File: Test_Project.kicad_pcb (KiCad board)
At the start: 2 copper layers, 4 parts, among them U1 STM32L081KZTx, U2 MIC2132YML

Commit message: Finished up schematic
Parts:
- added C10: 100nF, Test_Project_Lib:C_0603_1608Metric_Pad1.08x0.95mm_HandSolder, F.Cu at (116.6, 49.5)
- added C11: 1uF, Test_Project_Lib:C_0603_1608Metric_Pad1.08x0.95mm_HandSolder, F.Cu at (121.0, 39.5)
- added C12: 100nF, Test_Project_Lib:C_0603_1608Metric_Pad1.08x0.95mm_HandSolder, F.Cu at (121.0, 42.0)
- added C13: 1uF, Test_Project_Lib:C_0603_1608Metric_Pad1.08x0.95mm_HandSolder, F.Cu at (121.0, 44.5)
- added C14: 100nF, Test_Project_Lib:C_0603_1608Metric_Pad1.08x0.95mm_HandSolder, F.Cu at (121.0, 47.0)
- added C15: 22uF, Test_Project_Lib:C_0805_2012Metric_Pad1.18x1.45mm_HandSolder, F.Cu at (112.1, 27.9)
- added C16: 22uF, Test_Project_Lib:C_0805_2012Metric_Pad1.18x1.45mm_HandSolder, F.Cu at (112.1, 30.9)
- added C17: 100nF, Test_Project_Lib:C_0603_1608Metric_Pad1.08x0.95mm_HandSolder, F.Cu at (121.0, 49.5)
- added C18: ?uF, Test_Project_Lib:C_0603_1608Metric_Pad1.08x0.95mm_HandSolder, F.Cu at (125.3, 39.5)
- added C19: 4.7uF, Test_Project_Lib:C_0603_1608Metric_Pad1.08x0.95mm_HandSolder, F.Cu at (125.3, 42.0)
- added C2: 100nF, Test_Project_Lib:C_0603_1608Metric_Pad1.08x0.95mm_HandSolder, F.Cu at (169.1, 30.9)
- added C20: 4.7uF, Test_Project_Lib:C_0603_1608Metric_Pad1.08x0.95mm_HandSolder, F.Cu at (125.3, 44.5)
- added C21: 22uF, Test_Project_Lib:C_0805_2012Metric_Pad1.18x1.45mm_HandSolder, F.Cu at (112.1, 33.9)
- added C22: 22uF, Test_Project_Lib:C_0805_2012Metric_Pad1.18x1.45mm_HandSolder, F.Cu at (112.1, 36.9)
- added C23: 22uF, Test_Project_Lib:C_0805_2012Metric_Pad1.18x1.45mm_HandSolder, F.Cu at (112.1, 40.0)
- added C24: 22uF, Test_Project_Lib:C_0805_2012Metric_Pad1.18x1.45mm_HandSolder, F.Cu at (112.1, 43.0)
- added C25: 22uF, Test_Project_Lib:C_0805_2012Metric_Pad1.18x1.45mm_HandSolder, F.Cu at (112.1, 46.0)
- added C26: 22uF, Test_Project_Lib:C_0805_2012Metric_Pad1.18x1.45mm_HandSolder, F.Cu at (112.1, 49.0)
- added C27: 100uF, Test_Project_Lib:CP_Radial_D6.3mm_P2.50mm, F.Cu at (130.3, 42.1)
- added C28: 100nF, Test_Project_Lib:C_0603_1608Metric_Pad1.08x0.95mm_HandSolder, F.Cu at (142.7, 64.8)
- added C29: 1uF, Test_Project_Lib:C_0603_1608Metric_Pad1.08x0.95mm_HandSolder, F.Cu at (142.7, 67.3)
- added C3: 100nF, Test_Project_Lib:C_0603_1608Metric_Pad1.08x0.95mm_HandSolder, F.Cu at (169.1, 33.4)
- added C30: 1uF, Test_Project_Lib:C_0603_1608Metric_Pad1.08x0.95mm_HandSolder, F.Cu at (142.7, 69.8)
- added C31: 1uF, Test_Project_Lib:C_0603_1608Metric_Pad1.08x0.95mm_HandSolder, F.Cu at (169.1, 40.9)
- added C32: 1uF, Test_Project_Lib:C_0603_1608Metric_Pad1.08x0.95mm_HandSolder, F.Cu at (169.1, 43.4)
- added C4: 100nF, Test_Project_Lib:C_0603_1608Metric_Pad1.08x0.95mm_HandSolder, F.Cu at (169.1, 35.9)
- added C5: 1uF, Test_Project_Lib:C_0603_1608Metric_Pad1.08x0.95mm_HandSolder, F.Cu at (169.1, 38.4)
- added C6: 100pF, Test_Project_Lib:C_0603_1608Metric_Pad1.08x0.95mm_HandSolder, F.Cu at (116.6, 39.5)
- added C7: 100nF, Test_Project_Lib:C_0603_1608Metric_Pad1.08x0.95mm_HandSolder, F.Cu at (116.6, 42.0)
- added C8: 1uF, Test_Project_Lib:C_0603_1608Metric_Pad1.08x0.95mm_HandSolder, F.Cu at (116.6, 44.5)
- added C9: 100nF, Test_Project_Lib:C_0603_1608Metric_Pad1.08x0.95mm_HandSolder, F.Cu at (116.6, 47.0)
- added J2: Conn_01x02, Test_Project_Lib:PinHeader_1x02_P2.54mm_Vertical, F.Cu at (183.3, 69.4)
- added J3: Conn_01x03, Test_Project_Lib:PinHeader_1x03_P2.54mm_Vertical, F.Cu at (112.0, 64.9)
- added J4: Conn_01x03, Test_Project_Lib:PinHeader_1x03_P2.54mm_Vertical, F.Cu at (187.5, 29.4)
- added J5: Conn_01x04, Test_Project_Lib:PinHeader_1x04_P2.54mm_Vertical, F.Cu at (178.3, 29.4)
- added J6: Conn_01x04, Test_Project_Lib:PinHeader_1x04_P2.54mm_Vertical, F.Cu at (182.9, 29.4)
- added R1: 100k, Test_Project_Lib:R_0805_2012Metric_Pad1.20x1.40mm_HandSolder, F.Cu at (173.7, 28.6)
- added R10: 100k, Test_Project_Lib:R_0805_2012Metric_Pad1.20x1.40mm_HandSolder, F.Cu at (121.6, 36.7)
- added R11: 100k, Test_Project_Lib:R_0805_2012Metric_Pad1.20x1.40mm_HandSolder, F.Cu at (126.3, 27.9)
- added R12: 100k, Test_Project_Lib:R_0805_2012Metric_Pad1.20x1.40mm_HandSolder, F.Cu at (126.3, 30.8)
- added R13: 2.2Ω, Test_Project_Lib:R_0805_2012Metric_Pad1.20x1.40mm_HandSolder, F.Cu at (126.3, 33.8)
- added R14: 3.3k, Test_Project_Lib:R_0805_2012Metric_Pad1.20x1.40mm_HandSolder, F.Cu at (126.3, 36.7)
- added R15: 25.5 kΩ, Test_Project_Lib:R_0805_2012Metric_Pad1.20x1.40mm_HandSolder, F.Cu at (173.7, 34.5)
- added R16: 10k, Test_Project_Lib:R_0805_2012Metric_Pad1.20x1.40mm_HandSolder, F.Cu at (173.7, 37.5)
- added R17: 10k, Test_Project_Lib:R_0805_2012Metric_Pad1.20x1.40mm_HandSolder, F.Cu at (173.7, 40.4)
- added R18: 25.5 kΩ, Test_Project_Lib:R_0805_2012Metric_Pad1.20x1.40mm_HandSolder, F.Cu at (116.7, 64.1)
- added R19: 25.5 kΩ, Test_Project_Lib:R_0805_2012Metric_Pad1.20x1.40mm_HandSolder, F.Cu at (116.7, 67.0)
- added R2: 10k, Test_Project_Lib:R_0805_2012Metric_Pad1.20x1.40mm_HandSolder, F.Cu at (116.8, 27.9)
- added R3: 10k, Test_Project_Lib:R_0805_2012Metric_Pad1.20x1.40mm_HandSolder, F.Cu at (116.8, 30.8)
- added R4: 25.5 kΩ, Test_Project_Lib:R_0805_2012Metric_Pad1.20x1.40mm_HandSolder, F.Cu at (116.8, 33.8)
- added R5: 25.5 kΩ, Test_Project_Lib:R_0805_2012Metric_Pad1.20x1.40mm_HandSolder, F.Cu at (116.8, 36.7)
- added R6: 100k, Test_Project_Lib:R_0805_2012Metric_Pad1.20x1.40mm_HandSolder, F.Cu at (121.6, 27.9)
- added R7: 3.3k, Test_Project_Lib:R_0805_2012Metric_Pad1.20x1.40mm_HandSolder, F.Cu at (121.6, 30.8)
- added R8: 100k, Test_Project_Lib:R_0805_2012Metric_Pad1.20x1.40mm_HandSolder, F.Cu at (173.7, 31.6)
- added R9: 10kΩ, Test_Project_Lib:R_0805_2012Metric_Pad1.20x1.40mm_HandSolder, F.Cu at (121.6, 33.8)
- added U3: ~, Test_Project_Lib:SOT-23W_Handsoldering, F.Cu at (148.3, 66.0)
- moved U2 78.2 mm to (132.4, 30.1)
- moved C1 62.8 mm to (169.1, 28.4)
- moved U1 34.2 mm to (181.7, 45.0)
- moved J1 14.1 mm to (175.3, 61.1)
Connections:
- net Net-(U1-NRST) renamed /nRST
- C1 pad 2: GNDREF -> <NO NET>
- J1 pad 1: unconnected-(J1-Pad1) -> /12V
- J1 pad 3: unconnected-(J1-Pad3) -> <NO NET>
- U1 pad 1: unconnected-(U1-VDD-Pad1) -> /VDD_3V3
- U1 pad 11: unconnected-(U1-PA5-Pad11) -> /SPI_SCK
- U1 pad 12: unconnected-(U1-PA6-Pad12) -> /SPI_MISO
- U1 pad 13: unconnected-(U1-PA7-Pad13) -> /SPI_MOSI
- U1 pad 16: Net-(U1-VSS-Pad16) -> <NO NET>
- U1 pad 17: unconnected-(U1-VDD-Pad17) -> /VDD_3V3
- U1 pad 19: unconnected-(U1-PA9-Pad19) -> /USART_TX
- U1 pad 20: unconnected-(U1-PA10-Pad20) -> /USART_RX
- U1 pad 23: unconnected-(U1-PA13-Pad23) -> /SWDIO
- U1 pad 24: unconnected-(U1-PA14-Pad24) -> /SWCLK
- U1 pad 29: unconnected-(U1-PB6-Pad29) -> /I2C_SCL
- U1 pad 30: unconnected-(U1-PB7-Pad30) -> /I2C_SDA
- U1 pad 31: unconnected-(U1-BOOT0-Pad31) -> /Boot0
- U1 pad 32: Net-(U1-VSS-Pad16) -> <NO NET>
- U1 pad 5: unconnected-(U1-VDDA-Pad5) -> /VDD_3V3
- U1 pad 8: unconnected-(U1-PA2-Pad8) -> /LED_Data_Out (PWM)
- U2 pad 1: unconnected-(U2-CSN2-Pad1) -> <NO NET>
- U2 pad 10: unconnected-(U2-AGND-Pad10) -> <NO NET>
- U2 pad 11: unconnected-(U2-EXTVDD-Pad11) -> /VDD_5V
- U2 pad 12: unconnected-(U2-NPI-Pad12) -> Net-(U2-APO)
- U2 pad 13: unconnected-(U2-APO-Pad13) -> Net-(U2-APO)
- U2 pad 15: unconnected-(U2-OUTS-Pad15) -> Net-(U2-OUTS)
- U2 pad 16: unconnected-(U2-BST1-Pad16) -> Net-(U2-BST1)
- U2 pad 17: unconnected-(U2-DH1-Pad17) -> Net-(Q1-G)
- U2 pad 18: unconnected-(U2-SW1-Pad18) -> Net-(Q1-S)
- U2 pad 19: unconnected-(U2-DL1-Pad19) -> Net-(Q2-G)
- U2 pad 2: unconnected-(U2-CSP2-Pad2) -> Net-(Q3-S)
- U2 pad 20: unconnected-(U2-PGND-Pad20) -> <NO NET>
- U2 pad 21: unconnected-(U2-PVDD-Pad21) -> Net-(U2-PVDD)
- U2 pad 22: unconnected-(U2-DL2-Pad22) -> Net-(Q4-G)
- U2 pad 23: unconnected-(U2-SW2-Pad23) -> Net-(Q3-S)
- U2 pad 24: unconnected-(U2-DH2-Pad24) -> Net-(Q3-G)
- U2 pad 25: unconnected-(U2-BST2-Pad25) -> Net-(U2-BST2)
- U2 pad 26: unconnected-(U2-PG-Pad26) -> Net-(U2-PG)
- U2 pad 27: unconnected-(U2-RIP_INJ-Pad27) -> Net-(U2-RIP_INJ)
- U2 pad 28: unconnected-(U2-FBS-Pad28) -> Net-(U2-FBS)
- U2 pad 29: unconnected-(U2-GFB-Pad29) -> <NO NET>
- U2 pad 3: unconnected-(U2-CSN1-Pad3) -> <NO NET>
- U2 pad 30: unconnected-(U2-SS-Pad30) -> Net-(U2-SS)
- U2 pad 31: unconnected-(U2-FREQ-Pad31) -> Net-(U2-FREQ)
- U2 pad 32: unconnected-(U2-DROPP-Pad32) -> Net-(U2-DROPP)
- U2 pad 33: unconnected-(U2-PAD-Pad33) -> <NO NET>
- U2 pad 4: unconnected-(U2-CSP1-Pad4) -> Net-(Q1-S)
- U2 pad 5: unconnected-(U2-ILIM-Pad5) -> Net-(U2-ILIM)
- U2 pad 6: unconnected-(U2-CSH-Pad6) -> Net-(U2-CSH)
- U2 pad 7: unconnected-(U2-EN-Pad7) -> Net-(U2-EN)
- U2 pad 8: unconnected-(U2-VIN-Pad8) -> /Vin
- U2 pad 9: unconnected-(U2-VDD-Pad9) -> /Vin

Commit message: Started PCB layout
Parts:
- added C33: 22uF, Capacitor_SMD:C_0805_2012Metric_Pad1.18x1.45mm_HandSolder, F.Cu at (359.0, 120.6)
- added F1: 0678L9300-02, Test_Project_Lib:Fuse - 0678L9300-02, F.Cu at (323.5, 108.1)
- added L1: 2.2uH, Test_Project_Lib:SRP1265A, F.Cu at (368.9, 83.0)
- added L2: 2.2uH, Test_Project_Lib:SRP1265A, F.Cu at (368.4, 98.7)
- added Q1: NTTFS5C454NLTAG, Test_Project_Lib:NTTFS5C454NLTAG, F.Cu at (354.5, 79.3)
- added Q2: NTTFS5C454NLTAG, Test_Project_Lib:NTTFS5C454NLTAG, F.Cu at (354.4, 86.0)
- added Q3: NTTFS5C454NLTAG, Test_Project_Lib:NTTFS5C454NLTAG, F.Cu at (357.2, 101.7)
- added Q4: NTTFS5C454NLTAG, Test_Project_Lib:NTTFS5C454NLTAG, F.Cu at (357.2, 96.3)
- added Q5: BSS138-7-F, Test_Project_Lib:BSS138-7-F, F.Cu at (278.6, 129.3)
- added R20: 3.3k, Resistor_SMD:R_0805_2012Metric_Pad1.20x1.40mm_HandSolder, F.Cu at (351.7, 132.2)
- C1, C10, C11, C12, C13, C14, C17, C18, C19, C2, C20, C28, C29, C3, C30, C31, C32, C4, C5, C6, C7, C8, C9: footprint Test_Project_Lib:C_0603_1608Metric_Pad1.08x0.95mm_HandSolder -> Capacitor_SMD:C_0603_1608Metric_Pad1.08x0.95mm_HandSolder
- C15, C16, C21, C22, C23, C24, C25, C26: footprint Test_Project_Lib:C_0805_2012Metric_Pad1.18x1.45mm_HandSolder -> Capacitor_SMD:C_0805_2012Metric_Pad1.18x1.45mm_HandSolder
- C27: footprint Test_Project_Lib:CP_Radial_D6.3mm_P2.50mm -> Capacitor_THT:CP_Radial_D6.3mm_P2.50mm
- J1: footprint Test_Project_Lib:BarrelJack_GCT_DCJ200-10-A_Horizontal -> Connector_BarrelJack:BarrelJack_GCT_DCJ200-10-A_Horizontal
- J2: footprint Test_Project_Lib:PinHeader_1x02_P2.54mm_Vertical -> Connector_PinHeader_2.54mm:PinHeader_1x02_P2.54mm_Vertical
- J3: footprint Test_Project_Lib:PinHeader_1x03_P2.54mm_Vertical -> Connector_PinHeader_2.54mm:PinHeader_1x03_P2.54mm_Vertical
- J4: value Conn_01x03 -> Conn_01x04; footprint Test_Project_Lib:PinHeader_1x03_P2.54mm_Vertical -> Connector_PinHeader_2.54mm:PinHeader_1x04_P2.54mm_Vertical
- J5, J6: footprint Test_Project_Lib:PinHeader_1x04_P2.54mm_Vertical -> Connector_PinHeader_2.54mm:PinHeader_1x04_P2.54mm_Vertical
- R1: value 100k -> 1M; footprint Test_Project_Lib:R_0805_2012Metric_Pad1.20x1.40mm_HandSolder -> Resistor_SMD:R_0805_2012Metric_Pad1.20x1.40mm_HandSolder
- R10, R11, R12, R13, R14, R15, R16, R17, R18, R19, R2, R3, R4, R5, R6, R7, R8, R9: footprint Test_Project_Lib:R_0805_2012Metric_Pad1.20x1.40mm_HandSolder -> Resistor_SMD:R_0805_2012Metric_Pad1.20x1.40mm_HandSolder
- U1: footprint Test_Project_Lib:LQFP-32_7x7mm_P0.8mm -> Package_QFP:LQFP-32_7x7mm_P0.8mm
- U2: footprint Test_Project_Lib:QFN-32-1EP_5x5mm_P0.5mm_EP3.1x3.1mm -> Package_DFN_QFN:QFN-32-1EP_5x5mm_P0.5mm_EP3.1x3.1mm
- U3: value ~ -> AP2127N-3.3TRG1; footprint Test_Project_Lib:SOT-23W_Handsoldering -> Package_TO_SOT_SMD:SOT-23W_Handsoldering
- moved C24 282.3 mm to (387.9, 102.9), turned to -90 degrees
- moved C25 278.8 mm to (389.4, 74.8), turned to 90 degrees
- moved C26 278.1 mm to (384.9, 102.9), turned to -90 degrees
- moved C23 276.5 mm to (386.4, 74.8), turned to 90 degrees
- moved C12 268.5 mm to (382.5, 102.6), turned to -90 degrees
- moved C10 265.9 mm to (381.4, 75.0), turned to 90 degrees
- moved C13 265.5 mm to (380.0, 102.6), turned to -90 degrees
- moved C11 265.3 mm to (383.9, 75.0), turned to 90 degrees
- moved C27 256.1 mm to (381.6, 91.2), turned to 180 degrees
- moved C21 255.9 mm to (357.4, 106.6), turned to -90 degrees
- moved C22 252.1 mm to (354.4, 106.6), turned to -90 degrees
- moved C16 249.1 mm to (357.4, 74.0), turned to 90 degrees
- moved C15 246.6 mm to (354.4, 74.0), turned to 90 degrees
- moved R3 240.6 mm to (347.7, 98.6), turned to 90 degrees
- moved R2 237.2 mm to (347.7, 82.5), turned to -90 degrees
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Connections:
- C1 pad 2: <NO NET> -> GND
- C10 pad 2: <NO NET> -> GND
- C11 pad 2: <NO NET> -> GND
- C12 pad 2: <NO NET> -> GND
- C13 pad 2: <NO NET> -> GND
- C15 pad 2: <NO NET> -> GND
- C16 pad 2: <NO NET> -> GND
- C18 pad 2: <NO NET> -> GND
- C19 pad 2: <NO NET> -> GND
- C2 pad 2: <NO NET> -> GND
- C20 pad 2: <NO NET> -> GND
- C21 pad 2: <NO NET> -> GND
- C22 pad 2: <NO NET> -> GND
- C23 pad 2: <NO NET> -> GND
- C24 pad 2: <NO NET> -> GND
- C25 pad 2: <NO NET> -> GND
- C26 pad 2: <NO NET> -> GND
- C27 pad 2: <NO NET> -> GND
- C28 pad 2: <NO NET> -> GND
- C29 pad 2: <NO NET> -> GND
- C3 pad 2: <NO NET> -> GND
- C30 pad 2: <NO NET> -> GND
- C31 pad 1: Net-(C31-Pad1) -> /Vin_ADC
- C31 pad 2: <NO NET> -> GND
- C32 pad 1: Net-(C32-Pad1) -> /Vout_ADC
- C32 pad 2: <NO NET> -> GND
- C4 pad 2: <NO NET> -> GND
- C5 pad 2: <NO NET> -> GND
- C6 pad 1: <NO NET> -> GND
- C7 pad 1: <NO NET> -> GND
- J1 pad 3: <NO NET> -> GND
- J2 pad 2: <NO NET> -> GND
- J3 pad 2: unconnected-(J3-Pin_2-Pad2) -> Net-(J3-Pin_2)
- J3 pad 3: <NO NET> -> GND
- J4 pad 1: /USART_TX -> /VDD_3V3
- J4 pad 2: /USART_RX -> /USART_TX
- J4 pad 3: <NO NET> -> /USART_RX
- J5 pad 4: <NO NET> -> GND
- J6 pad 4: <NO NET> -> GND
- R1 pad 2: <NO NET> -> GND
- R14 pad 1: <NO NET> -> GND
- R15 pad 1: Net-(C32-Pad1) -> /Vout_ADC
- R16 pad 1: <NO NET> -> GND
- R16 pad 2: Net-(C31-Pad1) -> /Vin_ADC
- R17 pad 1: <NO NET> -> GND
- R17 pad 2: Net-(C32-Pad1) -> /Vout_ADC
- R19 pad 1: Net-(Q5-D) -> Net-(J3-Pin_2)
- R4 pad 1: <NO NET> -> GND
- R5 pad 1: <NO NET> -> GND
- R8 pad 1: Net-(C31-Pad1) -> /Vin_ADC
- U1 pad 15: unconnected-(U1-PB1-Pad15) -> /Vout_ADC
- U1 pad 16: <NO NET> -> GND
- U1 pad 32: <NO NET> -> GND
- U1 pad 6: unconnected-(U1-PA0-Pad6) -> /Bootloader_On_Reset
- U1 pad 9: unconnected-(U1-PA3-Pad9) -> /Vin_ADC
- U2 pad 1: <NO NET> -> GND
- U2 pad 10: <NO NET> -> GND
- U2 pad 20: <NO NET> -> GND
- U2 pad 29: <NO NET> -> GND
- U2 pad 3: <NO NET> -> GND
- U2 pad 33: <NO NET> -> GND
- U3 pad 1: <NO NET> -> GND

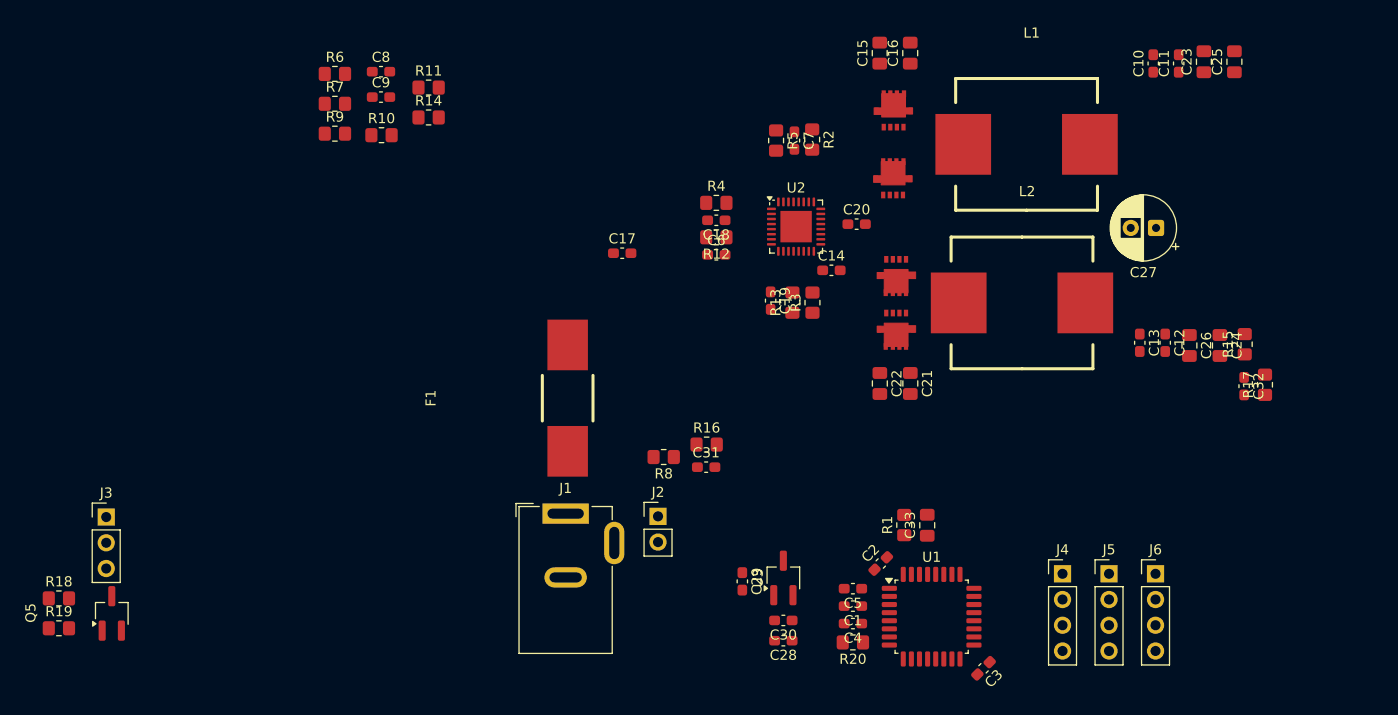
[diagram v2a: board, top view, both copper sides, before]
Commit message: Removed the 12V jack, added another 0.1" header in parallel so more current can be achieved if there are issues. Did most of the PCB layout. Updated some footprints
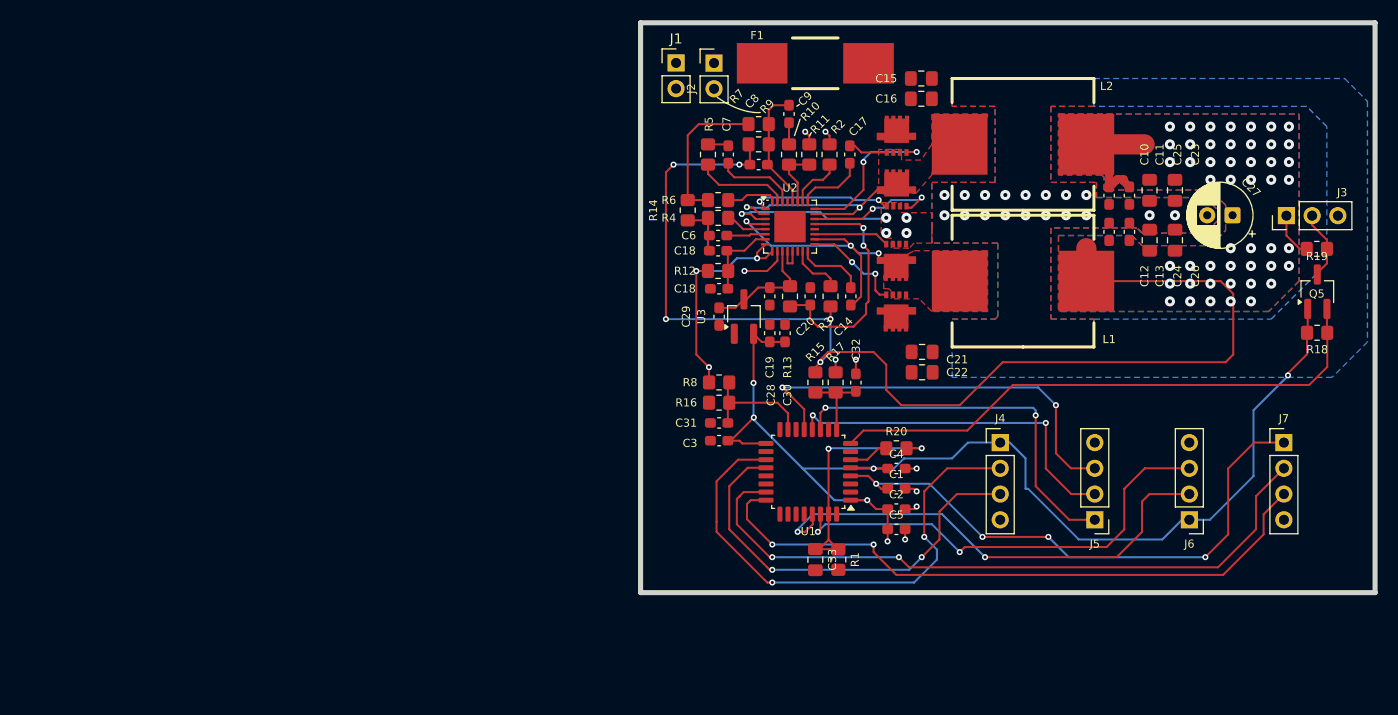
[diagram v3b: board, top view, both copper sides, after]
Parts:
- added C18: 100nF, Test_Project_Lib:C_0603_1608Metric_Pad1.08x0.95mm_HandSolder, F.Cu at (338.5, 97.2)
- added J7: Conn_01x04, Test_Project_Lib:PinHeader_1x04_P2.54mm_Vertical, F.Cu at (394.2, 112.4)
- C1, C10, C11, C12, C13, C14, C17, C18, C19, C2, C20, C28, C29, C3, C30, C31, C32, C4, C5, C6, C7, C8, C9: footprint Capacitor_SMD:C_0603_1608Metric_Pad1.08x0.95mm_HandSolder -> Test_Project_Lib:C_0603_1608Metric_Pad1.08x0.95mm_HandSolder
- C15, C16, C21, C22, C23, C24, C25, C26, C33: footprint Capacitor_SMD:C_0805_2012Metric_Pad1.18x1.45mm_HandSolder -> Test_Project_Lib:C_0805_2012Metric_Pad1.18x1.45mm_HandSolder
- C27: footprint Capacitor_THT:CP_Radial_D6.3mm_P2.50mm -> Test_Project_Lib:CP_Radial_D6.3mm_P2.50mm
- J1: value ~ -> Conn_01x02; footprint Connector_BarrelJack:BarrelJack_GCT_DCJ200-10-A_Horizontal -> Test_Project_Lib:PinHeader_1x02_P2.54mm_Vertical
- J2: footprint Connector_PinHeader_2.54mm:PinHeader_1x02_P2.54mm_Vertical -> Test_Project_Lib:PinHeader_1x02_P2.54mm_Vertical
- J3: footprint Connector_PinHeader_2.54mm:PinHeader_1x03_P2.54mm_Vertical -> Test_Project_Lib:PinHeader_1x03_P2.54mm_Vertical
- J4, J5, J6: footprint Connector_PinHeader_2.54mm:PinHeader_1x04_P2.54mm_Vertical -> Test_Project_Lib:PinHeader_1x04_P2.54mm_Vertical
- R1, R10, R11, R12, R13, R14, R15, R16, R17, R18, R19, R2, R20, R3, R4, R5, R6, R7, R8, R9: footprint Resistor_SMD:R_0805_2012Metric_Pad1.20x1.40mm_HandSolder -> Test_Project_Lib:R_0805_2012Metric_Pad1.20x1.40mm_HandSolder
- U1: footprint Package_QFP:LQFP-32_7x7mm_P0.8mm -> Test_Project_Lib:LQFP-32_7x7mm_P0.8mm
- U2: footprint Package_DFN_QFN:QFN-32-1EP_5x5mm_P0.5mm_EP3.1x3.1mm -> Test_Project_Lib:QFN-32-1EP_5x5mm_P0.5mm_EP3.1x3.1mm
- U3: footprint Package_TO_SOT_SMD:SOT-23W_Handsoldering -> Test_Project_Lib:SOT-23W_Handsoldering
- moved R19 129.7 mm to (397.5, 93.3), turned to 180 degrees
- moved R18 126.9 mm to (397.5, 101.6), turned to 180 degrees
- moved Q5 123.2 mm to (397.6, 97.5)
- moved J3 120.2 mm to (394.5, 90.0), turned to 90 degrees
- moved J1 45.8 mm to (334.2, 75.0)
- moved J2 45.1 mm to (338.0, 75.0)
- moved R15 42.6 mm to (348.0, 106.5)
- moved R17 42.4 mm to (350.0, 106.5), turned to -90 degrees
- moved R7 41.9 mm to (342.4, 81.0)
- moved R9 41.8 mm to (342.4, 83.0), turned to 180 degrees
- moved F1 41.1 mm to (348.0, 75.0), turned to 0 degrees
- moved C9 40.3 mm to (345.4, 80.0), turned to -90 degrees
- moved R10 40.3 mm to (345.4, 84.0), turned to 90 degrees
- moved R6 39.8 mm to (338.4, 88.5), turned to 180 degrees
- moved C8 38.4 mm to (342.4, 85.0)
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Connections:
- J1 pad 2: unconnected-(J1-Pad2) -> GND
- R11 pad 2: <NO NET> -> GND
- U1 pad 15: /Vout_ADC -> /Vin_ADC
- U1 pad 9: /Vin_ADC -> /Vout_ADC
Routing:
- net /Vout: track 0.00 -> 137.9 mm, vias 0 -> 53
- net /VDD_3V3: track 0.00 -> 117.3 mm, vias 0 -> 6
- net /SWDIO: track 0.00 -> 67.4 mm, vias 0 -> 2
- net /SWCLK: track 0.00 -> 63.7 mm, vias 0 -> 2
- net /nRST: track 0.00 -> 55.9 mm, vias 0 -> 4
- net /LED_Data_Out (PWM): track 0.00 -> 55.9 mm
- net GND: track 0.00 -> 52.1 mm, vias 0 -> 33
- net /USART_TX: track 0.00 -> 51.2 mm, vias 0 -> 2
- net /I2C_SCL: track 0.00 -> 48.5 mm, vias 0 -> 2
- net /I2C_SDA: track 0.00 -> 45.7 mm, vias 0 -> 2
- net /SPI_MOSI: track 0.00 -> 42.0 mm, vias 0 -> 2
- net /USART_RX: track 0.00 -> 41.7 mm, vias 0 -> 2
- net /SPI_SCK: track 0.00 -> 37.9 mm, vias 0 -> 2
- net /SPI_MISO: track 0.00 -> 35.1 mm, vias 0 -> 2
- net Net-(Q1-S): track 0.00 -> 27.7 mm, vias 0 -> 3
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- added copper zone on B.Cu, net /Vout
- added copper zone on F.Cu, net /Vout
- added copper zone on B.Cu, net GND
- added copper zone on F.Cu, net GND
- added copper zone on In1.Cu, net GND
- added copper zone on F.Cu, net Net-(Q1-S)
- added copper zone on F.Cu, net Net-(Q3-S)
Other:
- board outline added: 72.5 x 56.2 mm
- copper layers 2 -> 4
